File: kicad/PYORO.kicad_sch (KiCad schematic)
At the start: 98 parts, among them J1 BM06B-SRSS-TBLFSN, J2 Conn_01x04_Pin, J3 BM06B-SRSS-TBLFSN, J4 Conn_01x04_Pin, Q1 TEFT4300, Q2 TEFT4300, Q3 TEFT4300, Q4 TEFT4300, Q5 NMOS, Q6 NMOS, Q7 NMOS, Q8 NMOS, Q9 NMOS, U1 STM32H503CBTx, U2 L293D, U3 ICM-20948, U4 MC78LC18NTR, U5 LM1085-5.0, U6 AP2210N-3.3TRG1

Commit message: Modified LEDs, started Gate Driver, change H-Bridge
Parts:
- removed D18, D19: LED, symbol Device:LED
- removed R24, R25: 220, symbol Device:R
- added C27, C30, C34: 0.1uF, symbol Device:C
- added C28: 1uF, symbol Device:C
- added C29, C33: 4.7uF, symbol Device:C
- added C31, C32: 100uF, symbol Device:C
- added JP1: Jumper_2_Bridged, symbol Jumper:Jumper_2_Bridged
- added L1: 1mH, symbol Device:L
- added R27: 10k, symbol Device:R
- added SW1, SW2: SW_Push_Dual_x2, symbol Switch:SW_Push_Dual_x2
- added U10, U7: UCC27524, symbol UCC27524DSDR:UCC27524DSDR
- added U8, U9: ZXMHC3F381N8TC, SOIC_81N8TC_DIO, symbol ZXMHC3F381N8TC:ZXMHC3F381N8TC
- BT1: value Battery_Cell -> 2S LiPo
- C26: value C -> 2mF
- R26: value R -> 7
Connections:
- net +3.3VA: now also C26.2; no longer C26.1
- net +3V3: now also L1.1, SW2.1 (C); no longer R26.1
- net +5V: now also C29.2, C30.2, C31.1, C32.1, C33.2, C34.2, U10.6 (VDD), U7.6 (VDD), U8.7 (P1S/P2S), U9.7 (P1S/P2S)
- net GND: now also R26.1, C27.2, C28.2, C29.1, C30.1, C31.2, C32.2, C33.1, C34.1, JP1.1 (A), R27.2, SW1.2 (D), SW2.2 (D), U10.3 (GND), U7.3 (GND), U8.3 (N1S/N2S), U9.3 (N1S/N2S); no longer C11.2, C12.2, C13.2, C14.2, C15.2, C16.2, C26.2, R2.2, R3.2, R4.2, R5.2, U4.1 (GND)
- net ML_PWM: now also U7.2 (INA)
- net MR_PWM: now also U10.2 (INA)
- net UART_RX: now also U1.33 (PA12); no longer U1.25 (PB12)
- net BOOT0: now reaches U1.44 (BOOT0)
- net BOOT0: now also C28.1, R27.1
- net NRST: now reaches U1.7 (NRST)
- net NRST: now also C27.1, SW1.1 (C)
- net LED3: now reaches R19.1
- net LED3: now also U1.25 (PB12)
- net M1_L renamed ML_1
- net ML_1: now also U8.2 (N1D/P1D)
- net M1_R renamed MR_1
- net MR_1: now also U9.2 (N1D/P1D)
- net M2_L renamed ML_2
- net ML_2: now also U8.6 (N2D/P2D)
- net M2_R renamed MR_2
- net MR_2: now also U9.6 (N2D/P2D)
- new net: C26.1, L1.2
- new net: C15.2, C16.2, U4.1 (GND)
- new net GNDA: C11.2, C12.2, C13.2, C14.2, JP1.2 (B), R2.2, R3.2, R4.2, R5.2
- new net ML_DRIVEA: U7.7 (OUTA), U8.1 (N1G), U8.8 (P1G)
- new net ML_DRIVEB: U7.5 (OUTB), U8.4 (N2G), U8.5 (P2G)
- new net MR_DRIVEA: U10.7 (OUTA), U9.1 (N1G), U9.8 (P1G)
- new net MR_DRIVEB: U10.5 (OUTB), U9.4 (N2G), U9.5 (P2G)
- no-connect marks 7 -> 9
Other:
- note added: "Boot Address Selection"
- note added: "Decoupling Capacitors"
- note added: "Flash EN/Stored"
- note added: "Gate Driver, H-Bridge, Motor Encoder"
- note added: "Neopixels (RGB LED)"
- note added: "Reset Switch"
- note added: "Serial Wire-Debug"
- note added: "UART Support"
- note added: "VDDA Decoupling Capacitors"
- note removed: "... I could set the remaining GPIO pins to turn on/off LEDs"
- note removed: "Did not use a jumper for AGND"
- note removed: "Flash EN"
- note removed: "Flash Stored"
- note removed: "Motor Driver & Motor Encoder Headers"
- note removed: "Neopixels"
- note removed: "how da heck do people know the direction the motor will turn based on the current?"
- moved on the sheet: BT1, BZ1, C1, C10, C11, C12, C13, C14, C15, C16, C17, C18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

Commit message: Removed Enable pins for H-Bridge
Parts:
- added D18: 1655, 1655:LED_1655, symbol 1655:1655
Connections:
- net +5V: now also D18.3 (VDD)
- net GND: now also D18.1 (VSS)
- net at D3.2 (DIN): now also D18.4 (DOUT); no longer D2.4 (DOUT)
- net ML_BWD: no longer names the net of U1.40 (PB4(NJTRST))
- net ML_BWD: no longer U2.7 (2A)
- net ML_FWD: no longer names the net of U1.45 (PB8)
- net ML_FWD: no longer U2.2 (1A)
- net MR_BWD: no longer names the net of U1.42 (PB6)
- net MR_BWD: no longer U2.15 (4A)
- net MR_FWD: no longer names the net of U1.41 (PB5)
- net MR_FWD: no longer U2.10 (3A)
- new net: D18.2 (DIN), D2.4 (DOUT)
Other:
- moved on the sheet: BZ1, C1, C2, C3, C33, C34, C4, D1, D2, D3, D4, D5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
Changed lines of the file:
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@@
 	(title_block
 		(title "Pyoro Schematic")
-		(date "8/7/2025")
-		(rev "1.0")
+		(date "2025-11-27")
+		(rev "2.0")
 	)

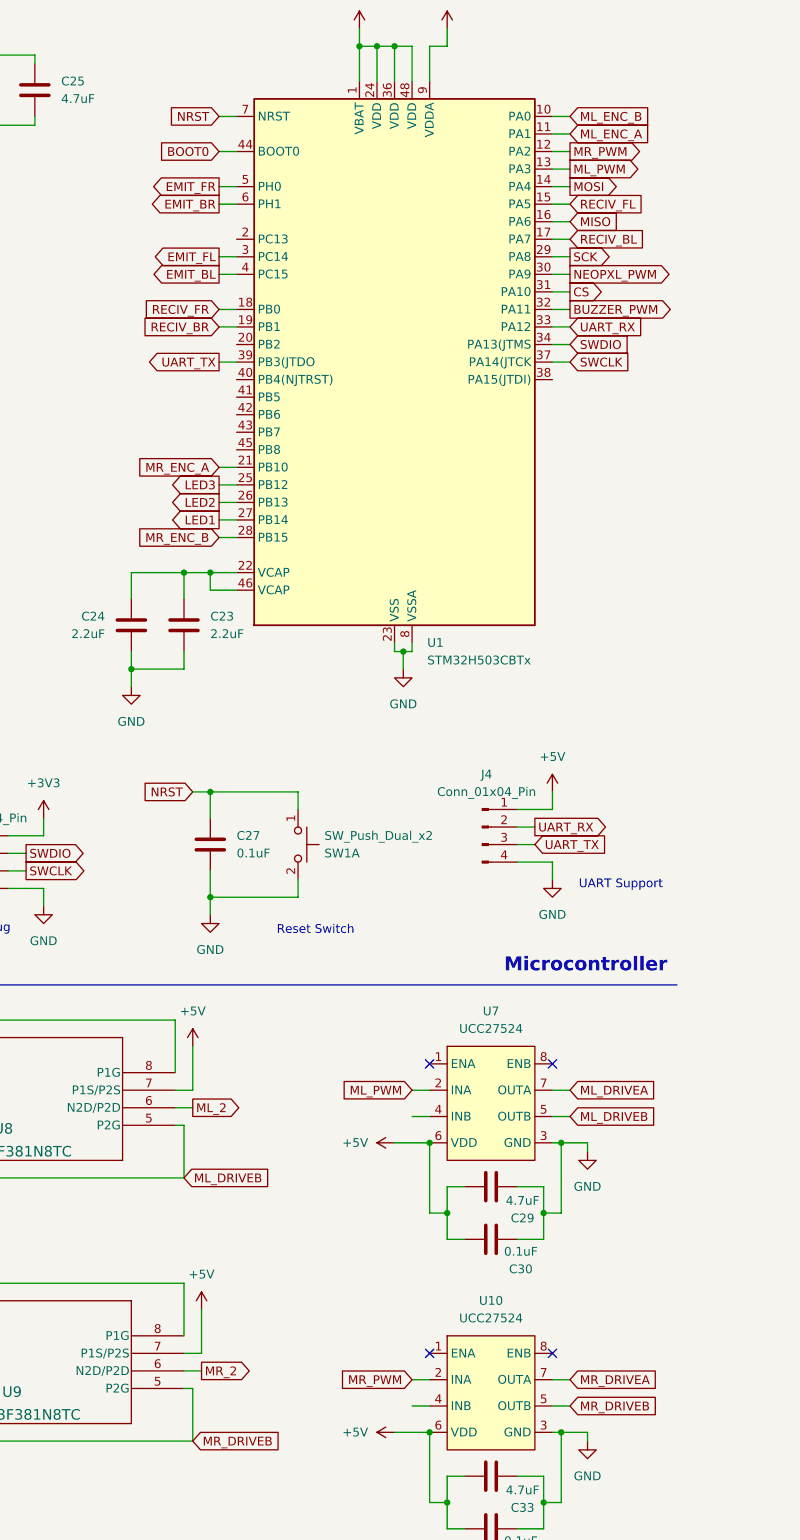
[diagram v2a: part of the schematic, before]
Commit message: Added 2 PWM channels for motors, and moved from UART3 to UART1
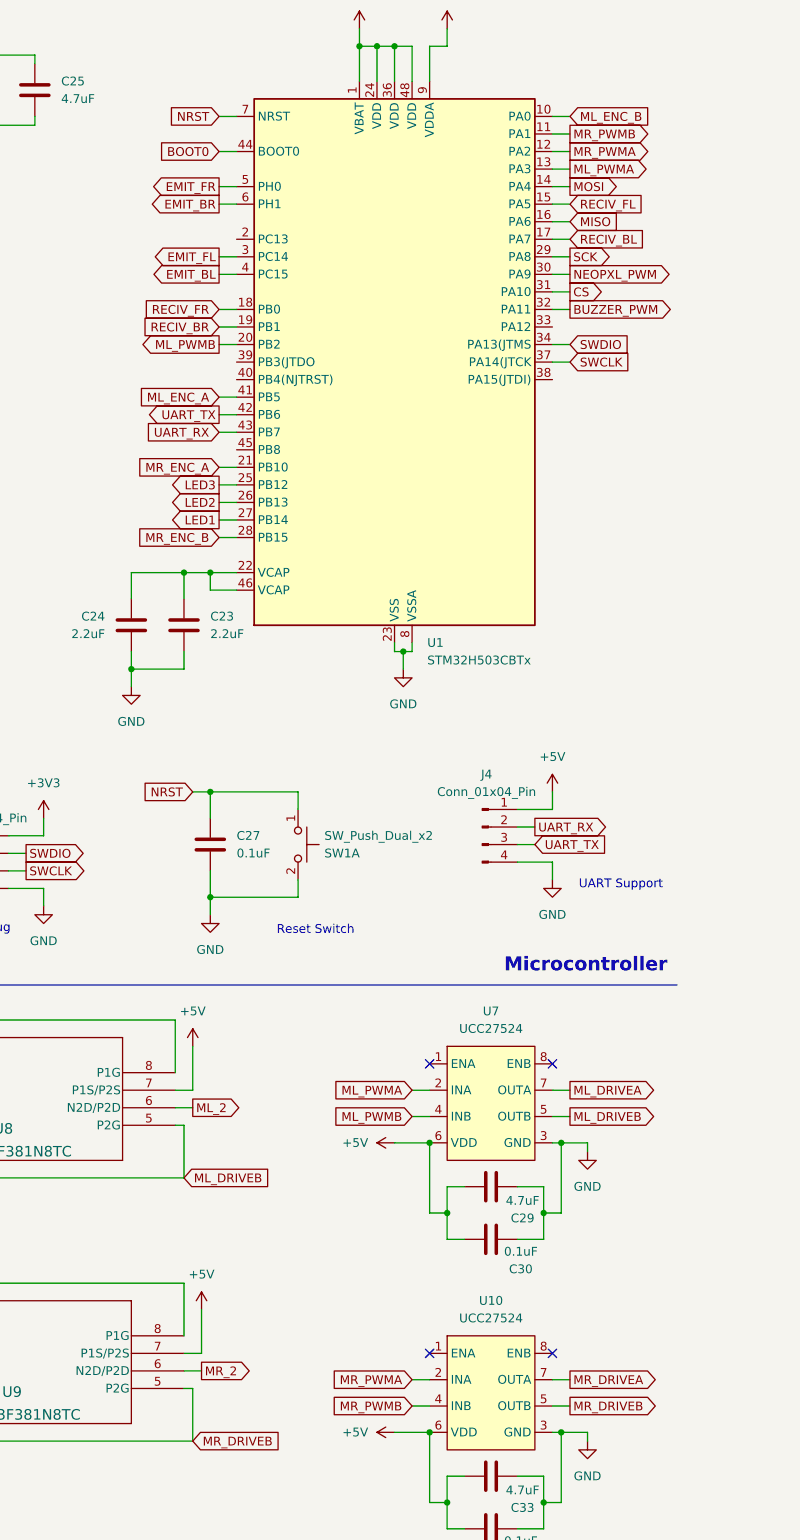
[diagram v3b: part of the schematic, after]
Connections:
- net ML_ENC_A: now also U1.41 (PB5); no longer U1.11 (PA1)
- net ML_PWM: no longer U1.13 (PA3), U7.2 (INA)
- net MR_PWM: no longer U1.12 (PA2), U10.2 (INA)
- net UART_RX: now also U1.43 (PB7); no longer U1.33 (PA12)
- net UART_TX: now also U1.42 (PB6); no longer U1.39 (PB3(JTDO)
- net ML_PWMB: now reaches U7.4 (INB)
- net ML_PWMB: now also U1.20 (PB2)
- net MR_PWMB: now reaches U10.4 (INB)
- net MR_PWMB: now also U1.11 (PA1)
- new net ML_PWMA: U1.13 (PA3), U7.2 (INA)
- new net MR_PWMA: U1.12 (PA2), U10.2 (INA)

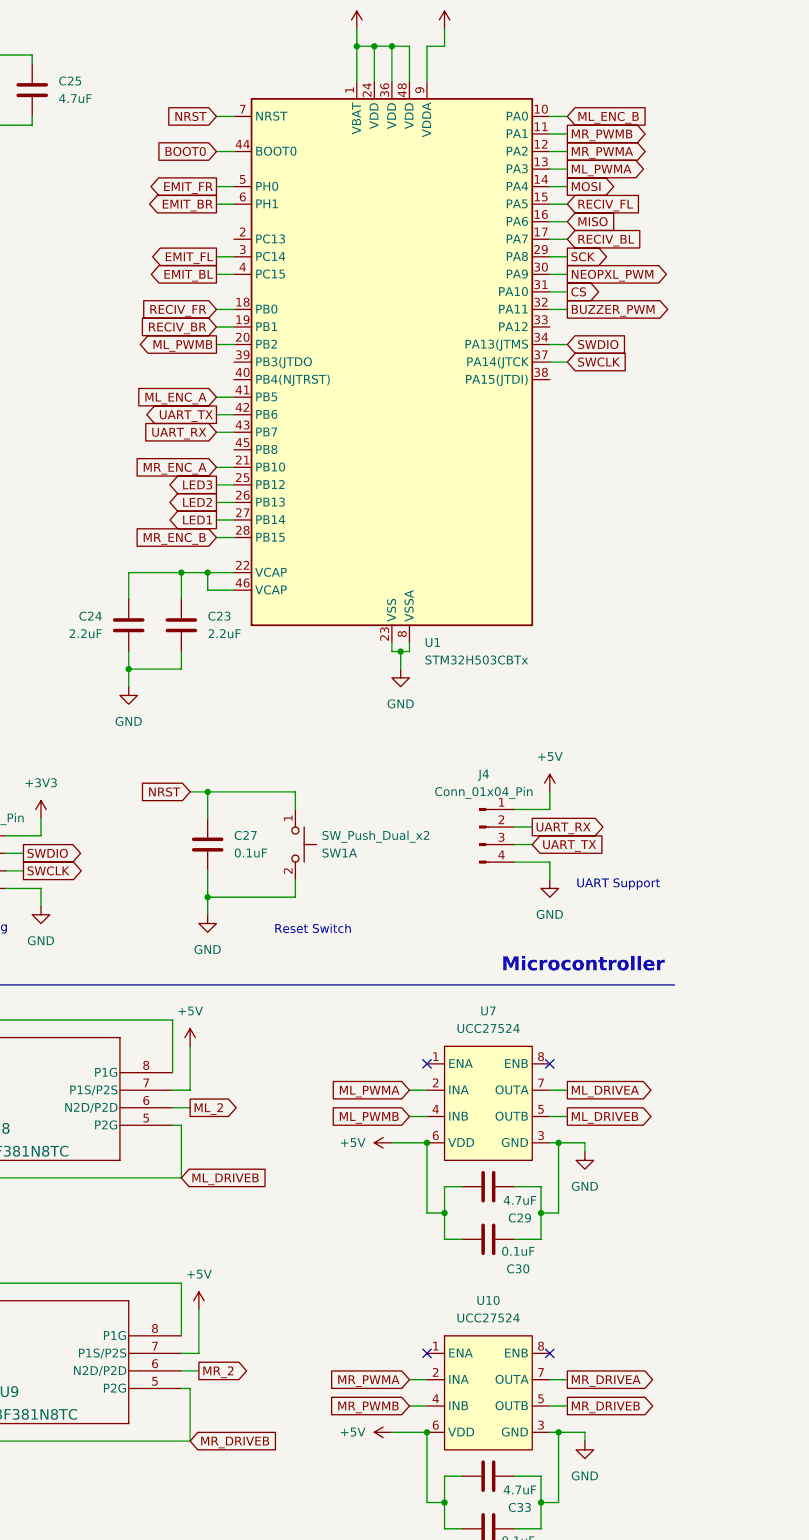
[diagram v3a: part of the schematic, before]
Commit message: Moved Motor PWM gen. to TIM1, and moved pin assignments
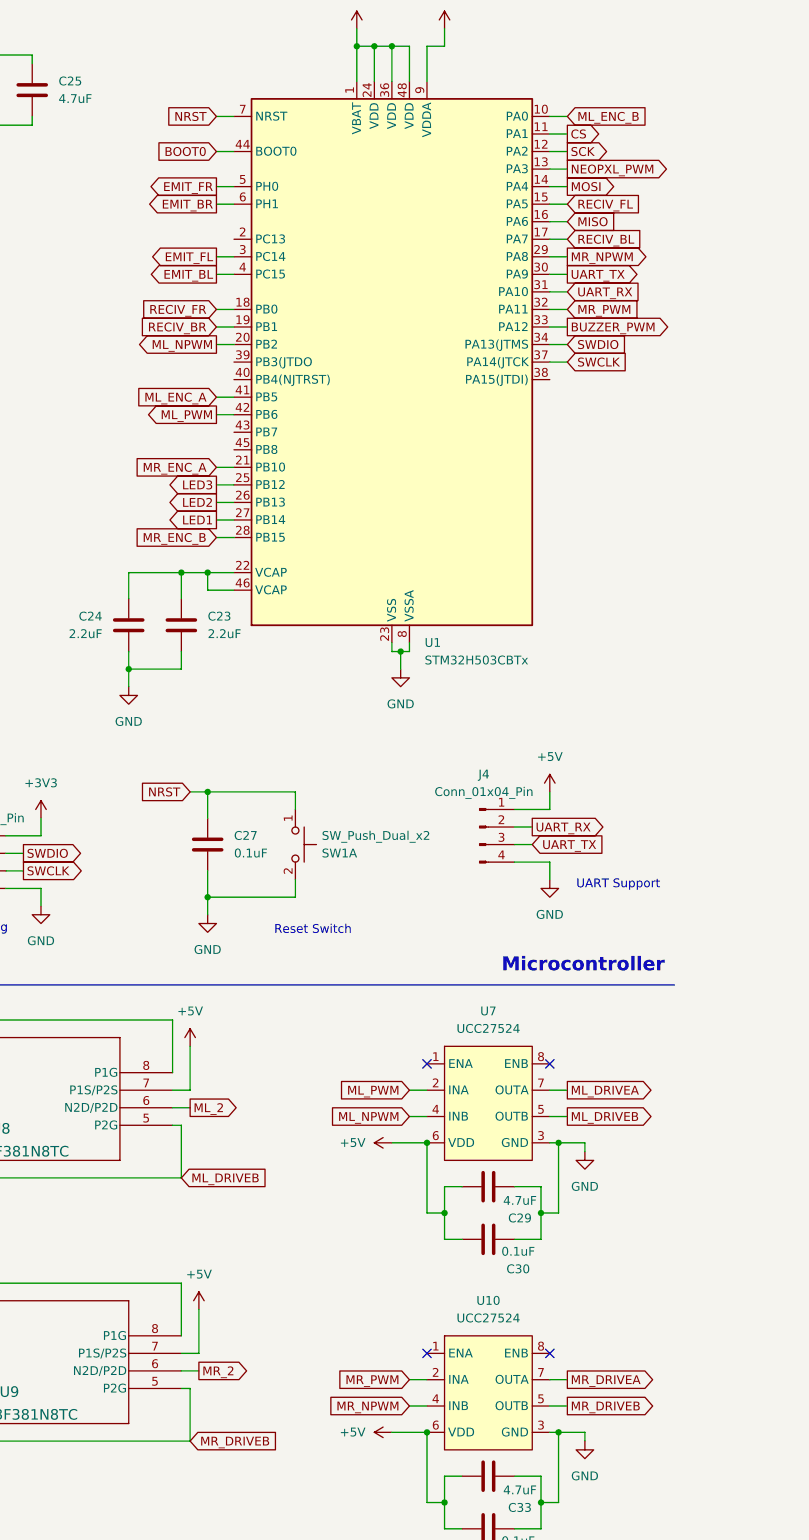
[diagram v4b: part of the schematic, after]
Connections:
- net BUZZER_PWM: now also U1.33 (PA12); no longer U1.32 (PA11)
- net CS: now also U1.11 (PA1); no longer U1.31 (PA10)
- net ML_PWM: now also U1.42 (PB6), U7.2 (INA)
- net MR_PWM: now also U1.32 (PA11), U10.2 (INA)
- net NEOPXL_PWM: now also U1.13 (PA3); no longer U1.30 (PA9)
- net SCK: now also U1.12 (PA2); no longer U1.29 (PA8)
- net UART_RX: now also U1.31 (PA10); no longer U1.43 (PB7)
- net UART_TX: now also U1.30 (PA9); no longer U1.42 (PB6)
- removed net ML_PWMA: U1.13 (PA3), U7.2 (INA)
- net ML_PWMB renamed ML_NPWM
- removed net MR_PWMA: U1.12 (PA2), U10.2 (INA)
- net MR_PWMB renamed MR_NPWM
- net MR_NPWM: now also U1.29 (PA8); no longer U1.11 (PA1)

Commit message: Completed pin assignments
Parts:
- removed C10: 1uF, symbol Device:C
- removed C9: 0.1uF, symbol Device:C
- removed U2: L293D, Package_DIP:DIP-16_W7.62mm, symbol Driver_Motor:L293D
- added D19, D20: LED, symbol Device:LED
- added R24, R25: 220, symbol Device:R
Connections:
- net GND: now also C15.2, C16.2, U4.1 (GND), D19.1 (K), D20.1 (K)
- net BIT2_LED: now reaches R23.1
- net BIT2_LED: now also U1.39 (PB3(JTDO)
- net RW_LED: now reaches U1.2 (PC13)
- net RW_LED: now also R21.1
- net BIT3_LED: now reaches U1.38 (PA15(JTDI))
- net BIT3_LED: now also R22.1
- net BIT1_LED: now reaches U1.40 (PB4(NJTRST))
- net BIT1_LED: now also R24.1
- net BIT0_LED: now reaches U1.43 (PB7)
- net BIT0_LED: now also R25.1
- net BACK_LED: now reaches U1.45 (PB8)
- net BACK_LED: now also R20.1
- net LED1 renamed FRONT_LED
- net LED2 renamed LEFT_LED
- net LED3 renamed RIGHT_LED
- new net: D20.2 (A), R25.2
- new net: D19.2 (A), R24.2
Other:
- moved on the sheet: D10, D11, D12, D13, D14, D15, D16, D17, R16, R17, R18, R19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
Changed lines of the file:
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@@
 	(title_block
 		(title "Pyoro Schematic")
-		(date "2025-11-27")
+		(date "2025-11-29")
 		(rev "2.0")
 	)
